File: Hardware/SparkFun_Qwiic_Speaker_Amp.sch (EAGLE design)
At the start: 53 parts, among them J1 QWIIC, J2 TRS_INPUT, J6 SCREW, U6 TPA2016D2

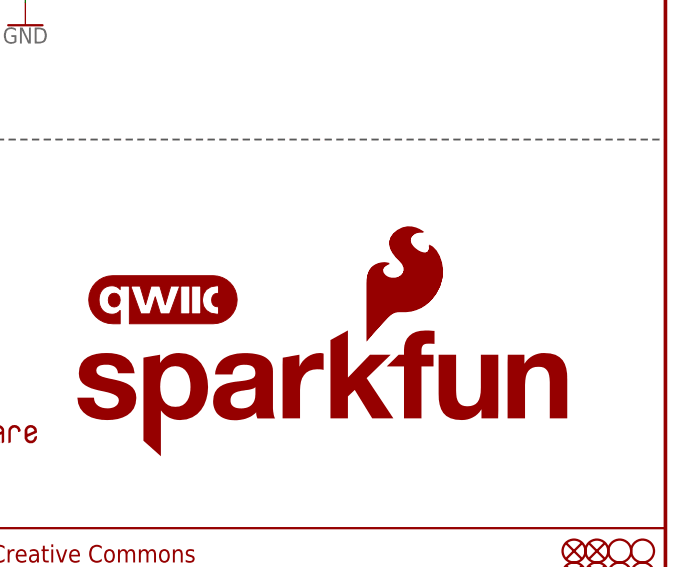
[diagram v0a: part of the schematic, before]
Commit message: Full SparkFun and flame logo on top silk
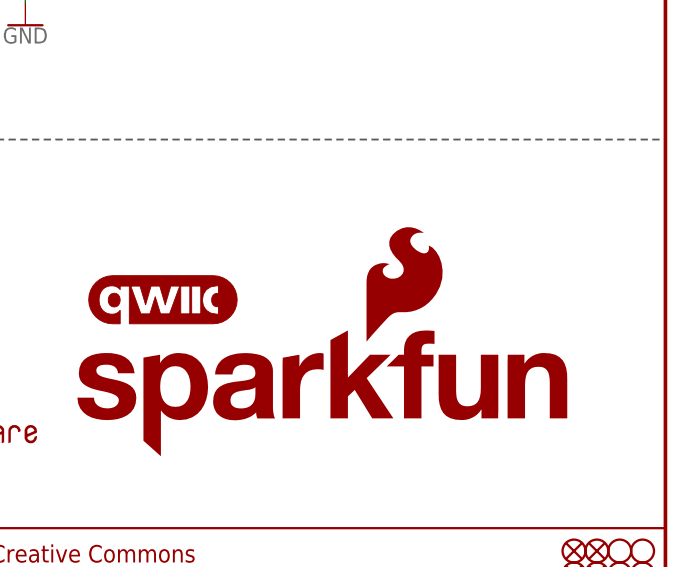
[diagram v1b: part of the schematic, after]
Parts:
- removed LOGO5: SFE_LOGO_FLAME.1_INCH, SparkFun-Aesthetics:SFE_LOGO_FLAME.1_INCH
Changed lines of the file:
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@@
 <part name="GND12" library="SparkFun-PowerSymbols" deviceset="GND" device=""/>
 <part name="GND13" library="SparkFun-PowerSymbols" deviceset="GND" device=""/>
-<part name="LOGO5" library="SparkFun-Aesthetics" deviceset="SFE_LOGO_FLAME" device=".1_INCH"/>
 <part name="SUPPLY5" library="SparkFun-PowerSymbols" deviceset="VCC" device=""/>
 <part name="GND15" library="SparkFun-PowerSymbols" deviceset="GND" device=""/>
@@
 <attribute name="VALUE" x="116.84" y="93.726" size="1.778" layer="96" font="vector" align="top-center"/>
 </instance>
-<instance part="LOGO5" gate="G$1" x="215.392" y="55.88" smashed="yes"/>
 <instance part="SUPPLY5" gate="G$1" x="81.28" y="167.64" smashed="yes" rot="MR0">
 <attribute name="VALUE" x="81.28" y="170.434" size="1.778" layer="96" font="vector" rot="MR0" align="bottom-center"/>

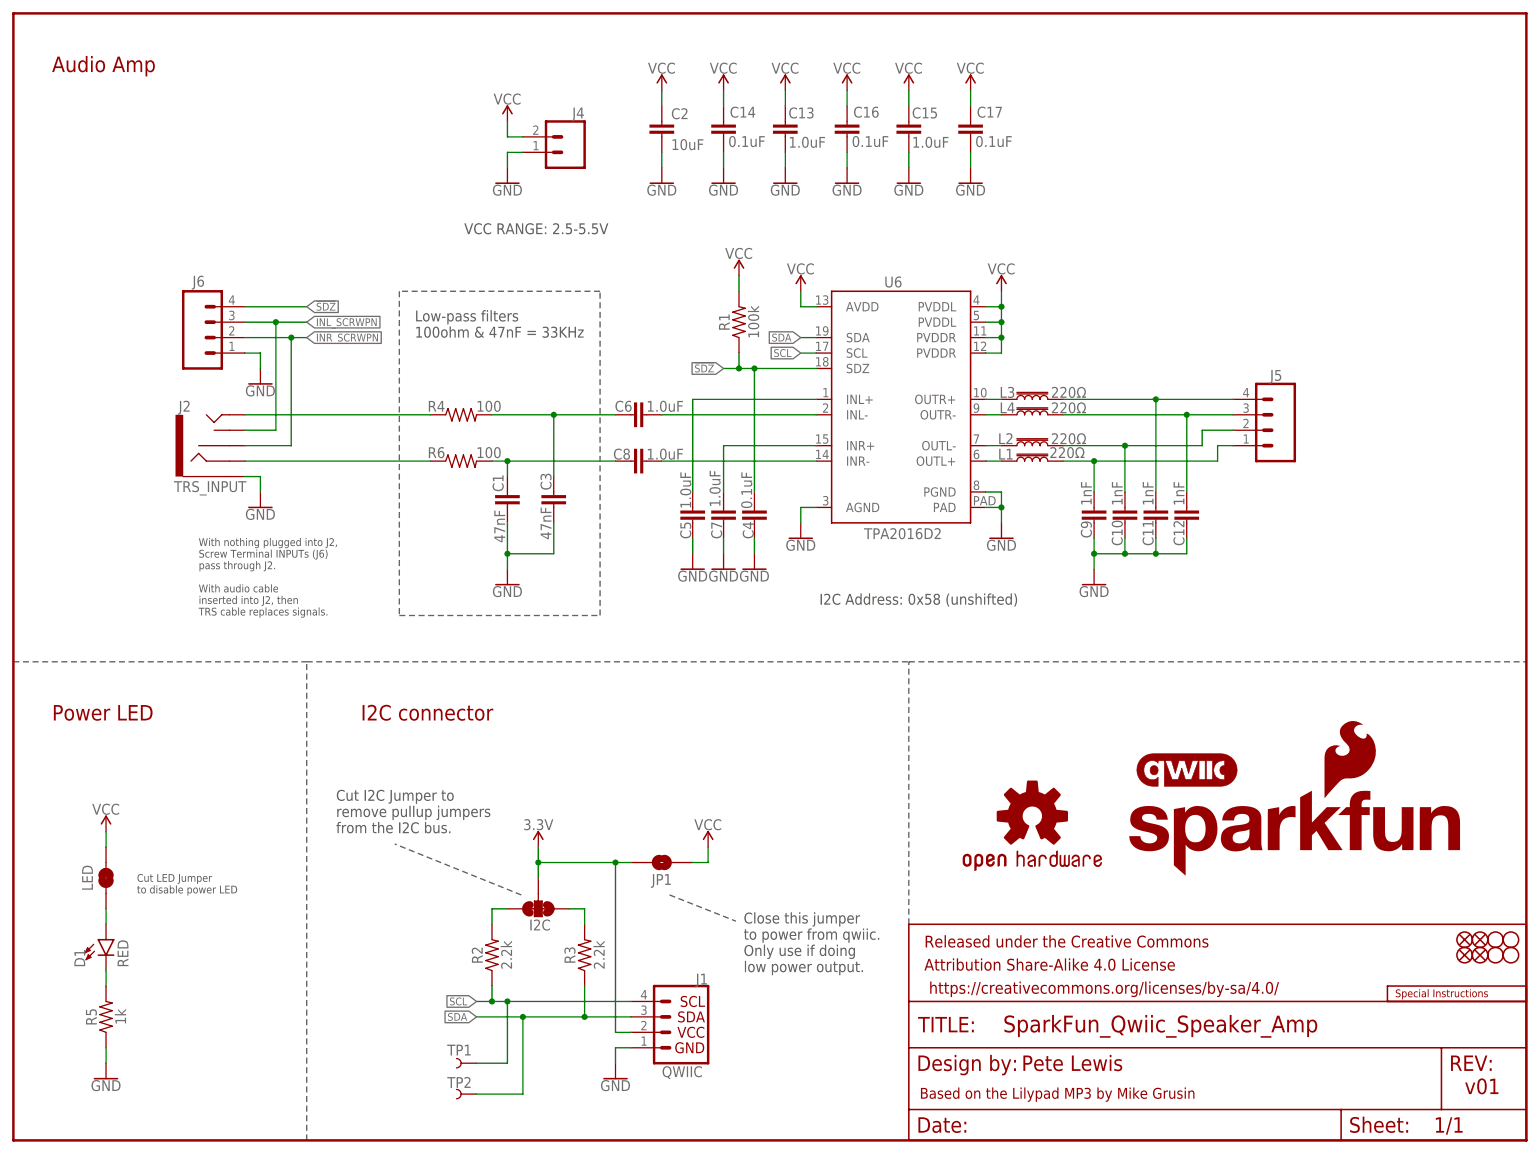
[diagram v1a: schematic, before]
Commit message: Added more VCC vias for connection to IC power pins.
-also thickened up the VCC traces to IC.
-bumped version to V10 in sch and brd
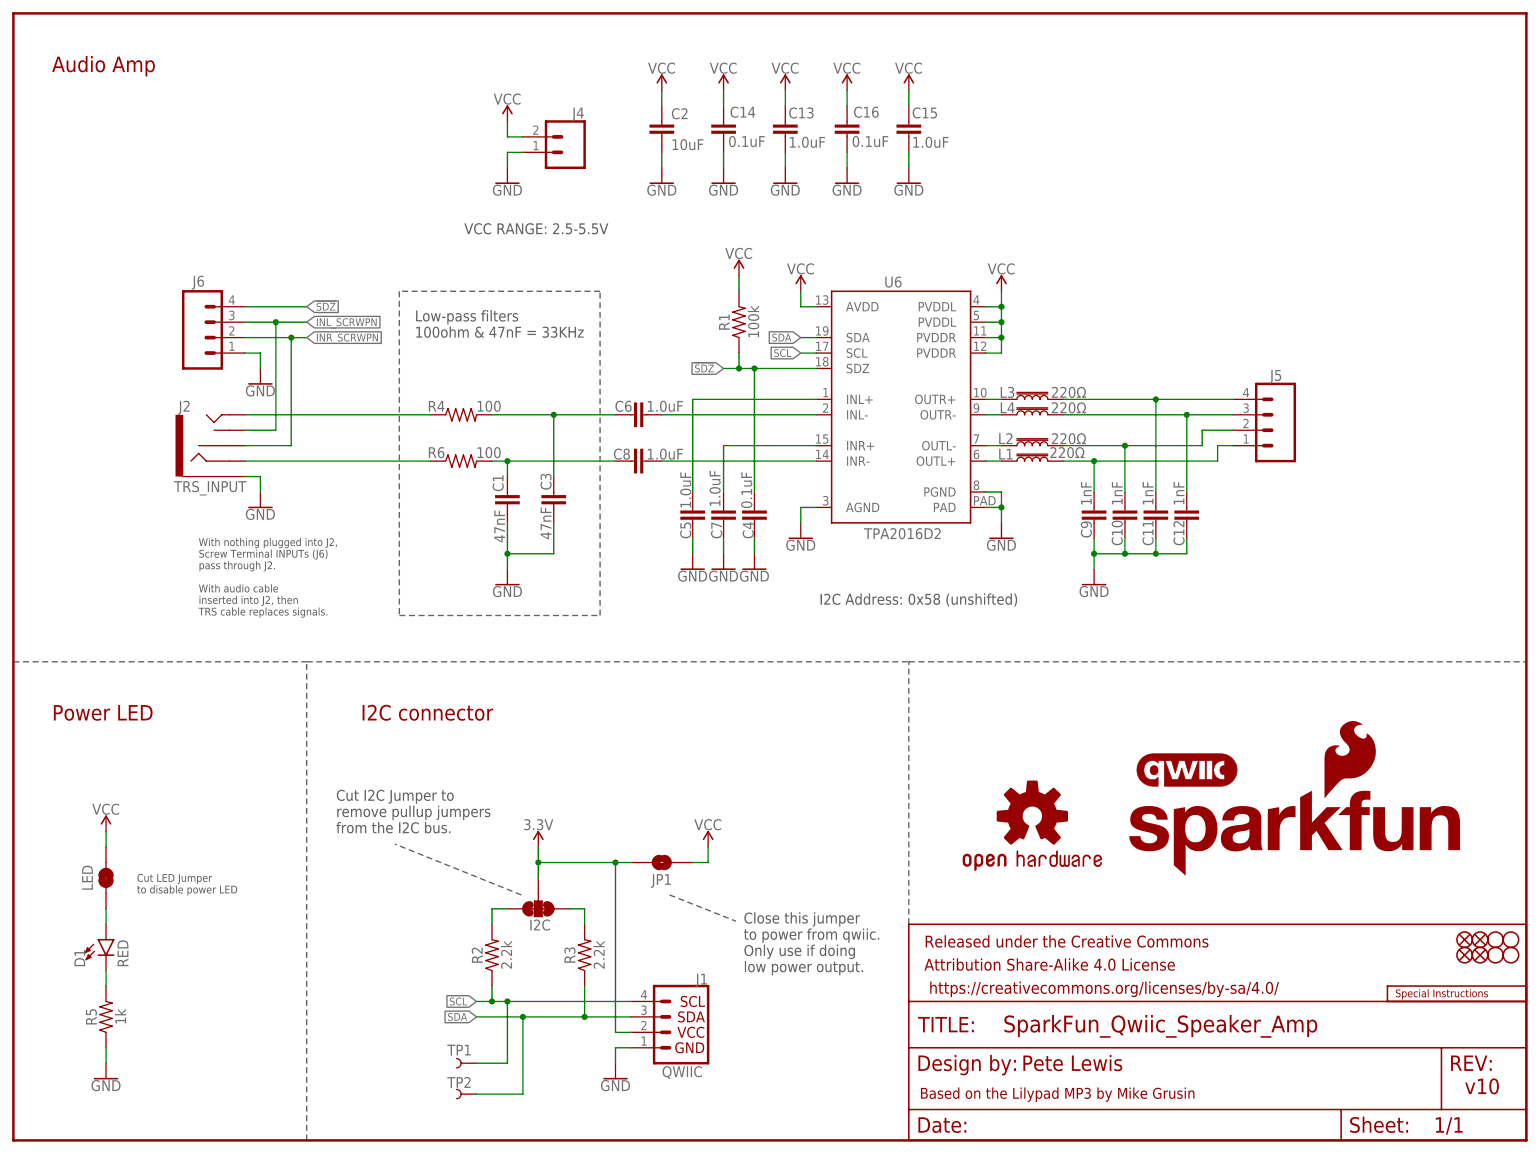
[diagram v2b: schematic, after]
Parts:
- removed C17: 0.1uF, SparkFun-Capacitors:0.1UF-0402T-16V-10%-X7R-WE
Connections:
- net GND: no longer C17.2
- net VCC: no longer C17.1
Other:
- note added: "v10"
- note removed: "v01"
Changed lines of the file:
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@@
 <part name="GND17" library="SparkFun-PowerSymbols" deviceset="GND" device=""/>
 <part name="C15" library="SparkFun-Capacitors" deviceset="1.0UF" device="-0402T-16V-10%" value="1.0uF"/>
-<part name="C17" library="SparkFun-Capacitors" deviceset="0.1UF" device="-0402T-16V-10%-X7R-WE" value="0.1uF"/>
-<part name="SUPPLY11" library="SparkFun-PowerSymbols" deviceset="VCC" device=""/>
-<part name="GND18" library="SparkFun-PowerSymbols" deviceset="GND" device=""/>
 <part name="JP1" library="SparkFun-Jumpers" deviceset="JUMPER-SMT_2_NO" device="_SILK" package3d_urn="urn:adsk.eagle:package:39279/1" value="JP1"/>
 <part name="SUPPLY12" library="SparkFun-PowerSymbols" deviceset="VCC" device=""/>
@@
 remove pullup jumpers
 from the I2C bus.</text>
-<text x="238.76" y="7.62" size="2.54" layer="94" font="vector">v01</text>
+<text x="238.76" y="7.62" size="2.54" layer="94" font="vector">v10</text>
 <text x="149.098" y="6.858" size="1.778" layer="94" font="vector">Based on the Lilypad MP3 by Mike Grusin</text>
 <wire x1="96.52" y1="139.7" x2="63.5" y2="139.7" width="0.2032" layer="97" style="shortdash"/>
@@
 <attribute name="VALUE" x="147.828" y="163.322" size="1.778" layer="96" font="vector"/>
 </instance>
-<instance part="C17" gate="G$1" x="157.48" y="165.1" smashed="yes">
-<attribute name="NAME" x="158.496" y="168.275" size="1.778" layer="95" font="vector"/>
-<attribute name="VALUE" x="158.242" y="163.449" size="1.778" layer="96" font="vector"/>
-</instance>
-<instance part="SUPPLY11" gate="G$1" x="157.48" y="172.72" smashed="yes">
-<attribute name="VALUE" x="157.48" y="175.514" size="1.778" layer="96" font="vector" align="bottom-center"/>
-</instance>
-<instance part="GND18" gate="1" x="157.48" y="157.48" smashed="yes">
-<attribute name="VALUE" x="157.48" y="157.226" size="1.778" layer="96" font="vector" align="top-center"/>
-</instance>
 <instance part="JP1" gate="G$1" x="106.68" y="45.72" smashed="yes">
 <attribute name="VALUE" x="106.68" y="42.926" size="1.778" layer="96" font="vector" align="center"/>
@@
 <pinref part="C15" gate="G$1" pin="2"/>
 </segment>
-<segment>
-<wire x1="157.48" y1="160.02" x2="157.48" y2="162.56" width="0.1524" layer="91"/>
-<pinref part="C17" gate="G$1" pin="2"/>
-<pinref part="GND18" gate="1" pin="GND"/>
-</segment>
 </net>
 <net name="SCL" class="0">
@@
 </segment>
 <segment>
-<pinref part="C17" gate="G$1" pin="1"/>
-<pinref part="SUPPLY11" gate="G$1" pin="VCC"/>
-<wire x1="157.48" y1="170.18" x2="157.48" y2="172.72" width="0.1524" layer="91"/>
-</segment>
-<segment>
